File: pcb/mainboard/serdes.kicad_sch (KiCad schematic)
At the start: 17 parts

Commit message: Continued initial work on main board
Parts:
- added C114, C115: 0.47 uF, symbol device:C
- added C116, C117, C118, C119, C120, C121: 0.1 uF, symbol device:C
- added D20, D21, D22, D23, D24, D25, D26, D27, D28, D29, D30: SZESD7471N2T5G, symbol device:D_TVS
- added J16, J17, J18, J19, J20, J21, J22, J23, J24, J25, J26: SMPM, symbol conn:CONN_COAXIAL
- added R121, R122, R123: DNP, symbol device:R
- added R161, R162: 1K, symbol device:R
- added U27: SIT9121AI-2BF-XXS200.000000G, symbol osc-azonenberg:OSC_LVDS_NOPAD
- added U28: SIT9121AI-2BF-XXS156.250000G, symbol osc-azonenberg:OSC_LVDS_NOPAD
- added U29: HMC675LP3E, symbol analog-azonenberg:HMC675LP3E
- C53, C54, C57, C58: renamed from C?; footprint azonenberg_pcb:EIA_0402_CAP_NOSILK -> (none)
- C55, C56: renamed from C?; footprint azonenberg_pcb:EIA_1206_CAP_NOSILK -> (none)
- J6: renamed from J?; footprint azonenberg_pcb:CONN_SFP+_AMPHENOL_UE76_A10_2000T -> (none)
- J7: renamed from J?; footprint azonenberg_pcb:CONN_SFP_CAGE_TE_2007194-1 -> (none)
- L1, L2: renamed from L?; footprint azonenberg_pcb:EIA_0805_INDUCTOR_NOSILK -> (none)
- R47, R48, R49, R50, R51, R52: renamed from R?; footprint azonenberg_pcb:EIA_0402_RES_NOSILK -> (none)
- U8: renamed from U?; footprint azonenberg_pcb:BGA_484_22x22_FULLARRAY_1MM -> (none)
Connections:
- net 3V3: now also C114.1, C115.1, R121.1, R161.1, R162.1, U27.1 (EN), U27.6 (VDD), U28.1 (EN), U28.6 (VDD), U29.16 (VCCI), U29.5 (VCCI)
- net GND: now also C114.2, C115.2, D20.1 (A1), D21.1 (A1), D22.1 (A1), D23.1 (A1), D24.1 (A1), D25.1 (A1), D26.1 (A1), D27.1 (A1), D28.1 (A1), D29.1 (A1), D30.1 (A1), J16.2 (Ext), J17.2 (Ext), J18.2 (Ext), J19.2 (Ext), J20.2 (Ext), J21.2 (Ext), J22.2 (Ext), J23.2 (Ext), J24.2 (Ext), J25.2 (Ext), J26.2 (Ext), R122.1, R123.2, U27.3 (GND), U28.3 (GND), U29.1 (VTP), U29.15 (RTN), U29.8 (NC/GND)
- net SFP_RS0: now also R161.2
- net SFP_RS1: now also R162.2
- net BERT_TX1_N: now reaches U8.A3 (GTX_TX_3_N)
- net BERT_TX1_N: now also D21.2 (A2), J17.1 (In)
- net BERT_TX1_P: now reaches U8.A4 (GTX_TX_3_P)
- net BERT_TX1_P: now also D20.2 (A2), J16.1 (In)
- net BERT_TX0_N: now reaches U8.B1 (GTX_TX_2_N)
- net BERT_TX0_N: now also D23.2 (A2), J19.1 (In)
- net BERT_TX0_P: now reaches U8.B2 (GTX_TX_2_P)
- net BERT_TX0_P: now also D22.2 (A2), J18.1 (In)
- net BERT_RX1_N: now reaches U8.B5 (GTX_RX_3_N)
- net BERT_RX1_N: now also D25.2 (A2), J21.1 (In)
- net BERT_RX1_P: now reaches U8.B6 (GTX_RX_3_P)
- net BERT_RX1_P: now also D24.2 (A2), J20.1 (In)
- net BERT_RX0_N: now reaches U8.C3 (GTX_RX_2_N)
- net BERT_RX0_N: now also D27.2 (A2), J23.1 (In)
- net BERT_RX0_P: now reaches U8.C4 (GTX_RX_2_P)
- net BERT_RX0_P: now also D26.2 (A2), J22.1 (In)
- net FASTSYNC_TX_N: now reaches U8.D1 (GTX_TX_1_N)
- net FASTSYNC_TX_N: now also D30.2 (A2), J26.1 (In)
- net FASTSYNC_TX_P: now reaches U8.D2 (GTX_TX_1_P)
- net FASTSYNC_TX_P: now also D29.2 (A2), J25.1 (In)
- net GTX_REFCLK_156M25_N: now reaches U8.D5 (GTX_REFCLK_0_N)
- net GTX_REFCLK_156M25_N: now also C119.2
- net GTX_REFCLK_156M25_P: now reaches U8.D6 (GTX_REFCLK_0_P)
- net GTX_REFCLK_156M25_P: now also C118.2
- net CDRTRIG_RX_N: now reaches U8.E3 (GTX_RX_1_N)
- net CDRTRIG_RX_N: now also C121.2
- net CDRTRIG_RX_P: now reaches U8.E4 (GTX_RX_1_P)
- net CDRTRIG_RX_P: now also C120.2
- net GTX_REFCLK_SPARE_N: now reaches U8.F5 (GTX_REFCLK_1_N)
- net GTX_REFCLK_SPARE_N: now also C117.2
- net GTX_REFCLK_SPARE_P: now reaches U8.F6 (GTX_REFCLK_1_P)
- net GTX_REFCLK_SPARE_P: now also C116.2
- new net: C119.1, U28.5 (OUT_N)
- new net: C118.1, U28.4 (OUT_P)
- new net: C117.1, U27.5 (OUT_N)
- new net: R123.1, U29.4 (VTN)
- new net: R121.2, U29.6 (LE_N)
- new net: R122.2, U29.7 (LE_P)
- new net: C116.1, U27.4 (OUT_P)
- new net 3V0_N: U29.13 (VEE), U29.PAD (VEE)
- new net CDRTRIG_IN: D28.2 (A2), J24.1 (In), U29.2 (IN_P)
- new net CDRTRIG_RX_AC_N: C121.1, U29.10 (Q_N)
- new net CDRTRIG_RX_AC_P: C120.1, U29.11 (Q_P)
- new net GTX_1V2: U29.12 (VCCO), U29.9 (VCCO)
- new net VREF_SERDESIN: U29.3 (IN_N)
- no-connect marks 0 -> 1
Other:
- note added: "Can use 156.25 for both Provide a second oscillator footprint just in case"
- note added: "Single ended CDR trigger input"
- note added: "TODO: decoupling for comparator"

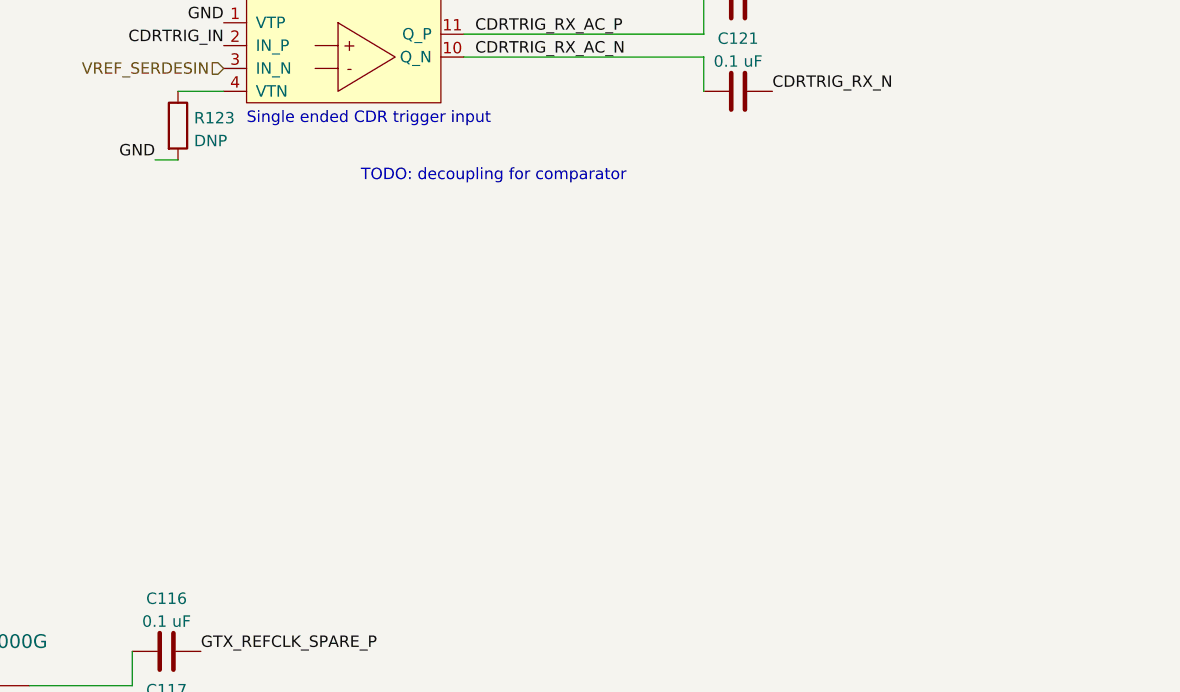
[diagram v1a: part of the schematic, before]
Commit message: Added missing decoupling caps to comparator
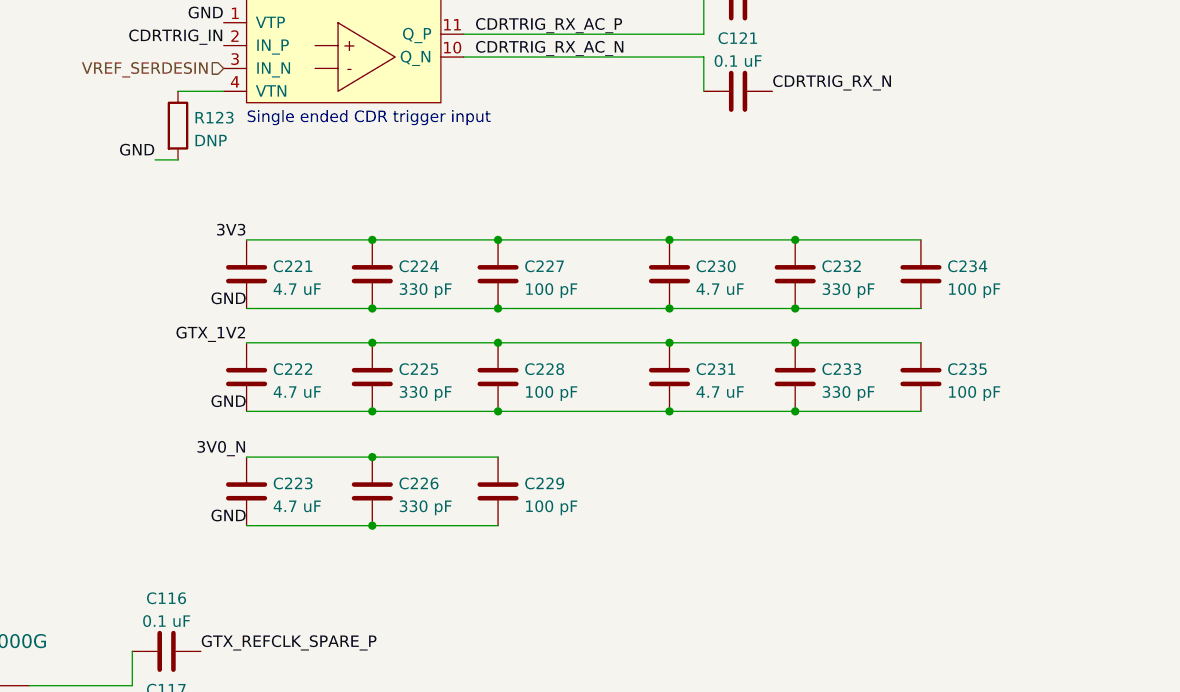
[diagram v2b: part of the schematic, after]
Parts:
- added C221, C222, C223, C230, C231: 4.7 uF, symbol device:C
- added C224, C225, C226, C232, C233: 330 pF, symbol device:C
- added C227, C228, C229, C234, C235: 100 pF, symbol device:C
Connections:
- net 3V0_N: now also C223.1, C226.1, C229.1
- net 3V3: now also C221.1, C224.1, C227.1, C230.1, C232.1, C234.1
- net GND: now also C221.2, C222.2, C223.2, C224.2, C225.2, C226.2, C227.2, C228.2, C229.2, C230.2, C231.2, C232.2, C233.2, C234.2, C235.2
- net GTX_1V2: now also C222.1, C225.1, C228.1, C231.1, C233.1, C235.1
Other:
- note removed: "TODO: decoupling for comparator"

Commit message: Calculated power monitor voltage divider
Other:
- company: (none) -> Antikernel Labs
- title: (none) -> Trigger Crossbar
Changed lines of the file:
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@@
 (kicad_sch (version 20211123) (generator eeschema)
   (paper "A3")
+  (title_block
+    (title "Trigger Crossbar")
+    (date "2023-12-17")
+    (rev "0.1")
+    (company "Antikernel Labs")
+    (comment 1 "Andrew D. Zonenberg")
+  )
   (junction (at 198.12 157.48) (diameter 0) (color 0 0 0 0)
   )

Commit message: Began assigning footprints
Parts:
- C114, C115, C116, C117, C118, C119, C120, C121, C224, C225, C226, C227, C228, C229, C232, C233, C234, C235, C53, C54, C57, C58: footprint (none) -> azonenberg_pcb:EIA_0402_CAP_NOSILK
- C221, C222, C223, C230, C231: footprint (none) -> azonenberg_pcb:EIA_0603_CAP_NOSILK
- C55, C56: footprint (none) -> azonenberg_pcb:EIA_0805_CAP_NOSILK
- D20, D21, D22, D23, D24, D25, D26, D27, D28, D29, D30: footprint (none) -> azonenberg_pcb:SOD882
- J6: footprint (none) -> azonenberg_pcb:CONN_SFP+_AMPHENOL_UE76_A10_2000T
- J7: footprint (none) -> azonenberg_pcb:CONN_SFP_CAGE_TE_2007194-1
- R121, R122, R123, R161, R162, R47, R48, R49, R50, R51, R52: footprint (none) -> azonenberg_pcb:EIA_0402_RES_NOSILK
- U27, U28: footprint (none) -> azonenberg_pcb:OSCILLATOR_LVDS_3.2x2.5
- U29: footprint (none) -> azonenberg_pcb:QFN_16_0.5MM_3x3MM
- U8: footprint (none) -> azonenberg_pcb:BGA_484_22x22_FULLARRAY_1MM

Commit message: Finished component footprint assignment, started some EM simulations. Ready for schematic review.
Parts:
- J16, J17, J18, J19, J20, J21, J22, J23, J24, J25, J26: footprint (none) -> azonenberg_pcb:CONN_SMPM_AMPHENOL_C925-197J-51PT
- L1, L2: footprint (none) -> azonenberg_pcb:EIA_0805_INDUCTOR_NOSILK
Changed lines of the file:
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@@
   (title_block
     (title "Trigger Crossbar")
-    (date "2023-12-17")
+    (date "2023-12-18")
     (rev "0.1")
     (company "Antikernel Labs")
@@
       (effects (font (size 1.27 1.27)) (justify left))
     )
-    (property "Footprint" "" (id 2) (at 62.23 170.18 0)
+    (property "Footprint" "azonenberg_pcb:CONN_SMPM_AMPHENOL_C925-197J-51PT" (id 2) (at 62.23 170.18 0)
       (effects (font (size 1.27 1.27)) hide)
     )
@@
       (effects (font (size 1.27 1.27)) (justify left))
     )
-    (property "Footprint" "" (id 2) (at 62.23 228.6 0)
+    (property "Footprint" "azonenberg_pcb:CONN_SMPM_AMPHENOL_C925-197J-51PT" (id 2) (at 62.23 228.6 0)
       (effects (font (size 1.27 1.27)) hide)
     )
@@
       (effects (font (size 1.016 1.016)))
     )
-    (property "Footprint" "" (id 2) (at 369.57 134.62 0)
+    (property "Footprint" "azonenberg_pcb:EIA_0805_INDUCTOR_NOSILK" (id 2) (at 369.57 134.62 0)
       (effects (font (size 1.524 1.524)) hide)
     )
@@
       (effects (font (size 1.27 1.27)) (justify left))
     )
-    (property "Footprint" "" (id 2) (at 62.23 217.17 0)
+    (property "Footprint" "azonenberg_pcb:CONN_SMPM_AMPHENOL_C925-197J-51PT" (id 2) (at 62.23 217.17 0)
       (effects (font (size 1.27 1.27)) hide)
     )
@@
       (effects (font (size 1.27 1.27)) (justify left))
     )
-    (property "Footprint" "" (id 2) (at 62.23 240.03 0)
+    (property "Footprint" "azonenberg_pcb:CONN_SMPM_AMPHENOL_C925-197J-51PT" (id 2) (at 62.23 240.03 0)
       (effects (font (size 1.27 1.27)) hide)
     )
@@
       (effects (font (size 1.27 1.27)) (justify left))
     )
-    (property "Footprint" "" (id 2) (at 62.23 193.04 0)
+    (property "Footprint" "azonenberg_pcb:CONN_SMPM_AMPHENOL_C925-197J-51PT" (id 2) (at 62.23 193.04 0)
       (effects (font (size 1.27 1.27)) hide)
     )
@@
       (effects (font (size 1.27 1.27)) (justify left))
     )
-    (property "Footprint" "" (id 2) (at 62.23 252.73 0)
+    (property "Footprint" "azonenberg_pcb:CONN_SMPM_AMPHENOL_C925-197J-51PT" (id 2) (at 62.23 252.73 0)
       (effects (font (size 1.27 1.27)) hide)
     )
@@
       (effects (font (size 1.27 1.27)) (justify left))
     )
-    (property "Footprint" "" (id 2) (at 121.92 158.75 0)
+    (property "Footprint" "azonenberg_pcb:CONN_SMPM_AMPHENOL_C925-197J-51PT" (id 2) (at 121.92 158.75 0)
       (effects (font (size 1.27 1.27)) hide)
     )
@@
       (effects (font (size 1.27 1.27)) (justify left))
     )
-    (property "Footprint" "" (id 2) (at 62.23 181.61 0)
+    (property "Footprint" "azonenberg_pcb:CONN_SMPM_AMPHENOL_C925-197J-51PT" (id 2) (at 62.23 181.61 0)
       (effects (font (size 1.27 1.27)) hide)
     )
@@
       (effects (font (size 1.27 1.27)) (justify left))
     )
-    (property "Footprint" "" (id 2) (at 62.23 158.75 0)
+    (property "Footprint" "azonenberg_pcb:CONN_SMPM_AMPHENOL_C925-197J-51PT" (id 2) (at 62.23 158.75 0)
       (effects (font (size 1.27 1.27)) hide)
     )
@@
       (effects (font (size 1.27 1.27)) (justify left))
     )
-    (property "Footprint" "" (id 2) (at 121.92 170.18 0)
+    (property "Footprint" "azonenberg_pcb:CONN_SMPM_AMPHENOL_C925-197J-51PT" (id 2) (at 121.92 170.18 0)
       (effects (font (size 1.27 1.27)) hide)
     )
@@
       (effects (font (size 1.016 1.016)))
     )
-    (property "Footprint" "" (id 2) (at 369.57 114.3 0)
+    (property "Footprint" "azonenberg_pcb:EIA_0805_INDUCTOR_NOSILK" (id 2) (at 369.57 114.3 0)
       (effects (font (size 1.524 1.524)) hide)
     )
@@
       (effects (font (size 1.27 1.27)) (justify left))
     )
-    (property "Footprint" "" (id 2) (at 62.23 205.74 0)
-      (effects (font (size 1.27 1.27)) hide)
-    )
+    (property "Footprint" "azonenberg_pcb:CONN_SMPM_AMPHENOL_C925-197J-51PT" (id 2) (at 62.23 205.74 0)
+      (effects (font (size 1.27 1.27)) hide)
+    )

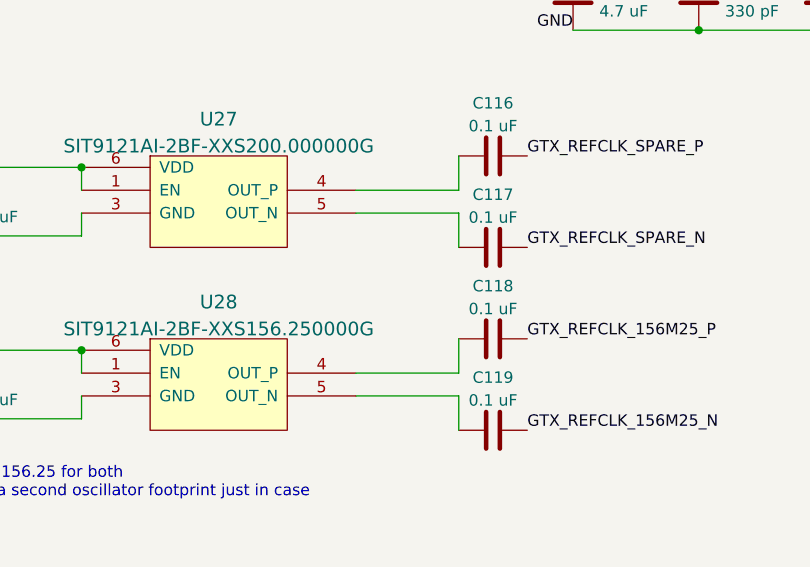
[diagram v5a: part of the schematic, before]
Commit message: Finished initial schematic review of trigger crossbar mainboard
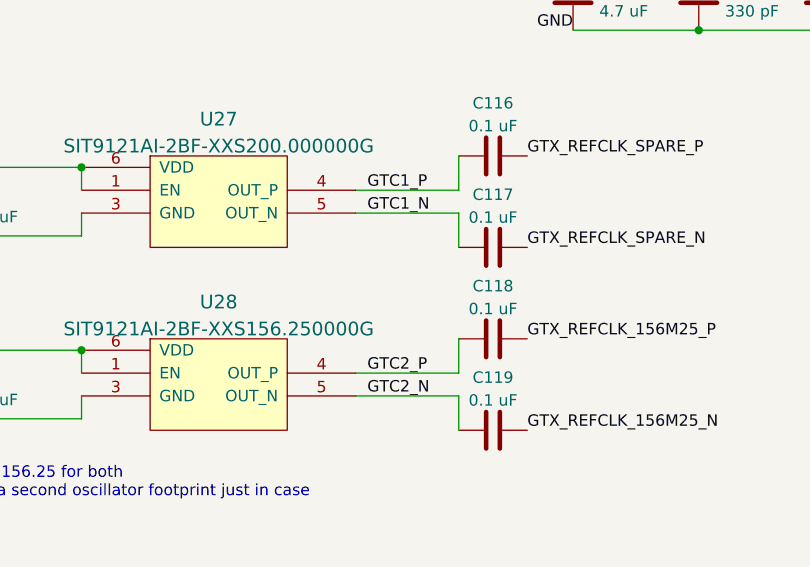
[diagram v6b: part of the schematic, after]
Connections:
- net GTC2_N: now reaches C119.1, U28.5 (OUT_N)
- net GTC2_P: now reaches C118.1, U28.4 (OUT_P)
- net GTC1_N: now reaches C117.1, U27.5 (OUT_N)
- net GTC1_P: now reaches C116.1, U27.4 (OUT_P)
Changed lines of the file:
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@@
   (title_block
     (title "Trigger Crossbar")
-    (date "2023-12-18")
+    (date "2023-12-19")
     (rev "0.1")
     (company "Antikernel Labs")
@@
     (effects (font (size 1.27 1.27)) (justify right bottom))
   )
+  (label "GTC1_N" (at 147.32 201.93 0)
+    (effects (font (size 1.27 1.27)) (justify left bottom))
+  )
   (label "SFP_I2C_SCL" (at 377.19 163.83 180)
     (effects (font (size 1.27 1.27)) (justify right bottom))
@@
     (effects (font (size 1.27 1.27)) (justify right bottom))
   )
+  (label "GTC2_N" (at 147.32 222.25 0)
+    (effects (font (size 1.27 1.27)) (justify left bottom))
+  )
   (label "GTX_REFCLK_156M25_N" (at 52.07 82.55 180)
     (effects (font (size 1.27 1.27)) (justify right bottom))
@@
     (effects (font (size 1.27 1.27)) (justify right bottom))
   )
+  (label "GTC1_P" (at 147.32 199.39 0)
+    (effects (font (size 1.27 1.27)) (justify left bottom))
+  )
   (label "FASTSYNC_TX_N" (at 52.07 52.07 180)
     (effects (font (size 1.27 1.27)) (justify right bottom))
   )
+  (label "GTC2_P" (at 147.32 219.71 0)
+    (effects (font (size 1.27 1.27)) (justify left bottom))
+  )
   (label "SFP_RS1" (at 365.76 64.77 180)

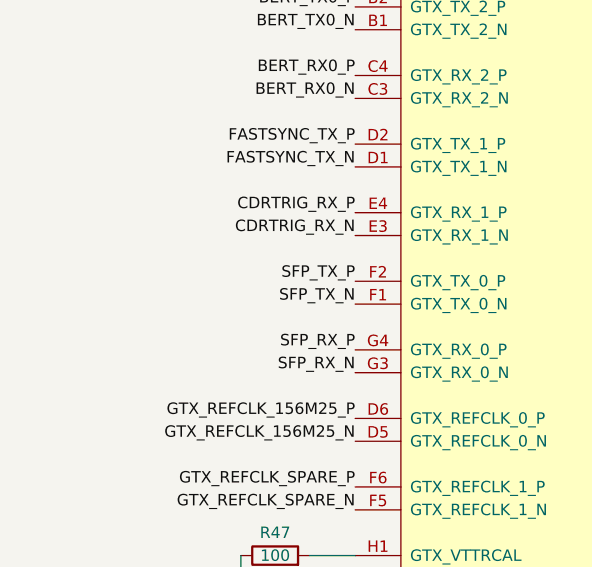
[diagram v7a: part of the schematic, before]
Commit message: Initial FPGA routing
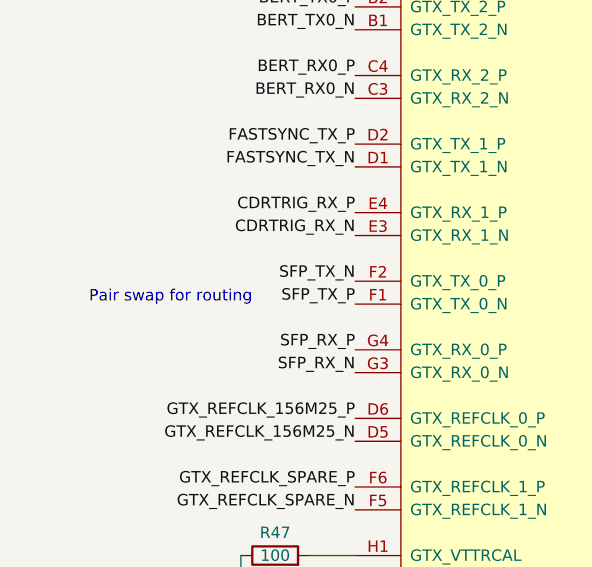
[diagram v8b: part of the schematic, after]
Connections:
- net SFP_TX_N: now also U8.F2 (GTX_TX_0_P); no longer U8.F1 (GTX_TX_0_N)
- net SFP_TX_P: now also U8.F1 (GTX_TX_0_N); no longer U8.F2 (GTX_TX_0_P)
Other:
- note added: "Pair swap for routing"
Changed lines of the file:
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@@
   (title_block
     (title "Trigger Crossbar")
-    (date "2023-12-20")
+    (date "2023-12-22")
     (rev "0.1")
     (company "Antikernel Labs")
@@
     (effects (font (size 1.27 1.27)) (justify left bottom))
   )
+  (text "Pair swap for routing" (at 40.64 67.31 180)
+    (effects (font (size 1.27 1.27)) (justify right bottom))
+  )
   (text "SFP+ power filtering" (at 347.98 152.4 0)
     (effects (font (size 1.27 1.27)) (justify left bottom))
@@
     (effects (font (size 1.27 1.27)) (justify right bottom))
   )
-  (label "SFP_TX_N" (at 52.07 67.31 180)
+  (label "SFP_TX_N" (at 52.07 64.77 180)
     (effects (font (size 1.27 1.27)) (justify right bottom))
   )
@@
     (effects (font (size 1.27 1.27)) (justify left bottom))
   )
-  (label "SFP_TX_P" (at 52.07 64.77 180)
-    (effects (font (size 1.27 1.27)) (justify right bottom))
-  )
+  (label "SFP_TX_P" (at 52.07 67.31 180)
+    (effects (font (size 1.27 1.27)) (justify right bottom))
+  )
